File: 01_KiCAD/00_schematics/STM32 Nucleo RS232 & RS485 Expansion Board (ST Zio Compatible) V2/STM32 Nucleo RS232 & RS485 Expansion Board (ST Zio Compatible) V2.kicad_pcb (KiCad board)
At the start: 4 copper layers, 70 x 133.4 mm, 190 parts, among them CN10 Conn_02x17_Odd_Even, CN7 Conn_02x10_Odd_Even, CN8 Conn_02x08_Odd_Even, CN9 Conn_02x15_Odd_Even, IC1 REG103GA-A, J1 1190299, J10 DIR, J11 TERM_TX, J12 TERM_RX, J13 SLR, J2 CONN D-SUB PLUG 9POS TH, J3 TCVR_PWR, J4 TX_LED, J5 RX_LED, J6 SW_ENA, J7 MODE0, J8 MODE1, J9 MODE2, Q1 BSS84, Q2 BSS84, U1 TPS2117DRLR, U10 SN74LVC2G14DBV, U11 SN74LVC2G14DBV, U2 THVD4431RHAR, U3 SN74LVC2G14DBV, U4 SN74LVC245ADBR, U5 SN74LVC2G14DBV, U6 SN74LVC2G14DBV, U7 SN74LVC2G14DBV, U8 SN74LVC2G14DBV, U9 SN74LVC2G14DBV

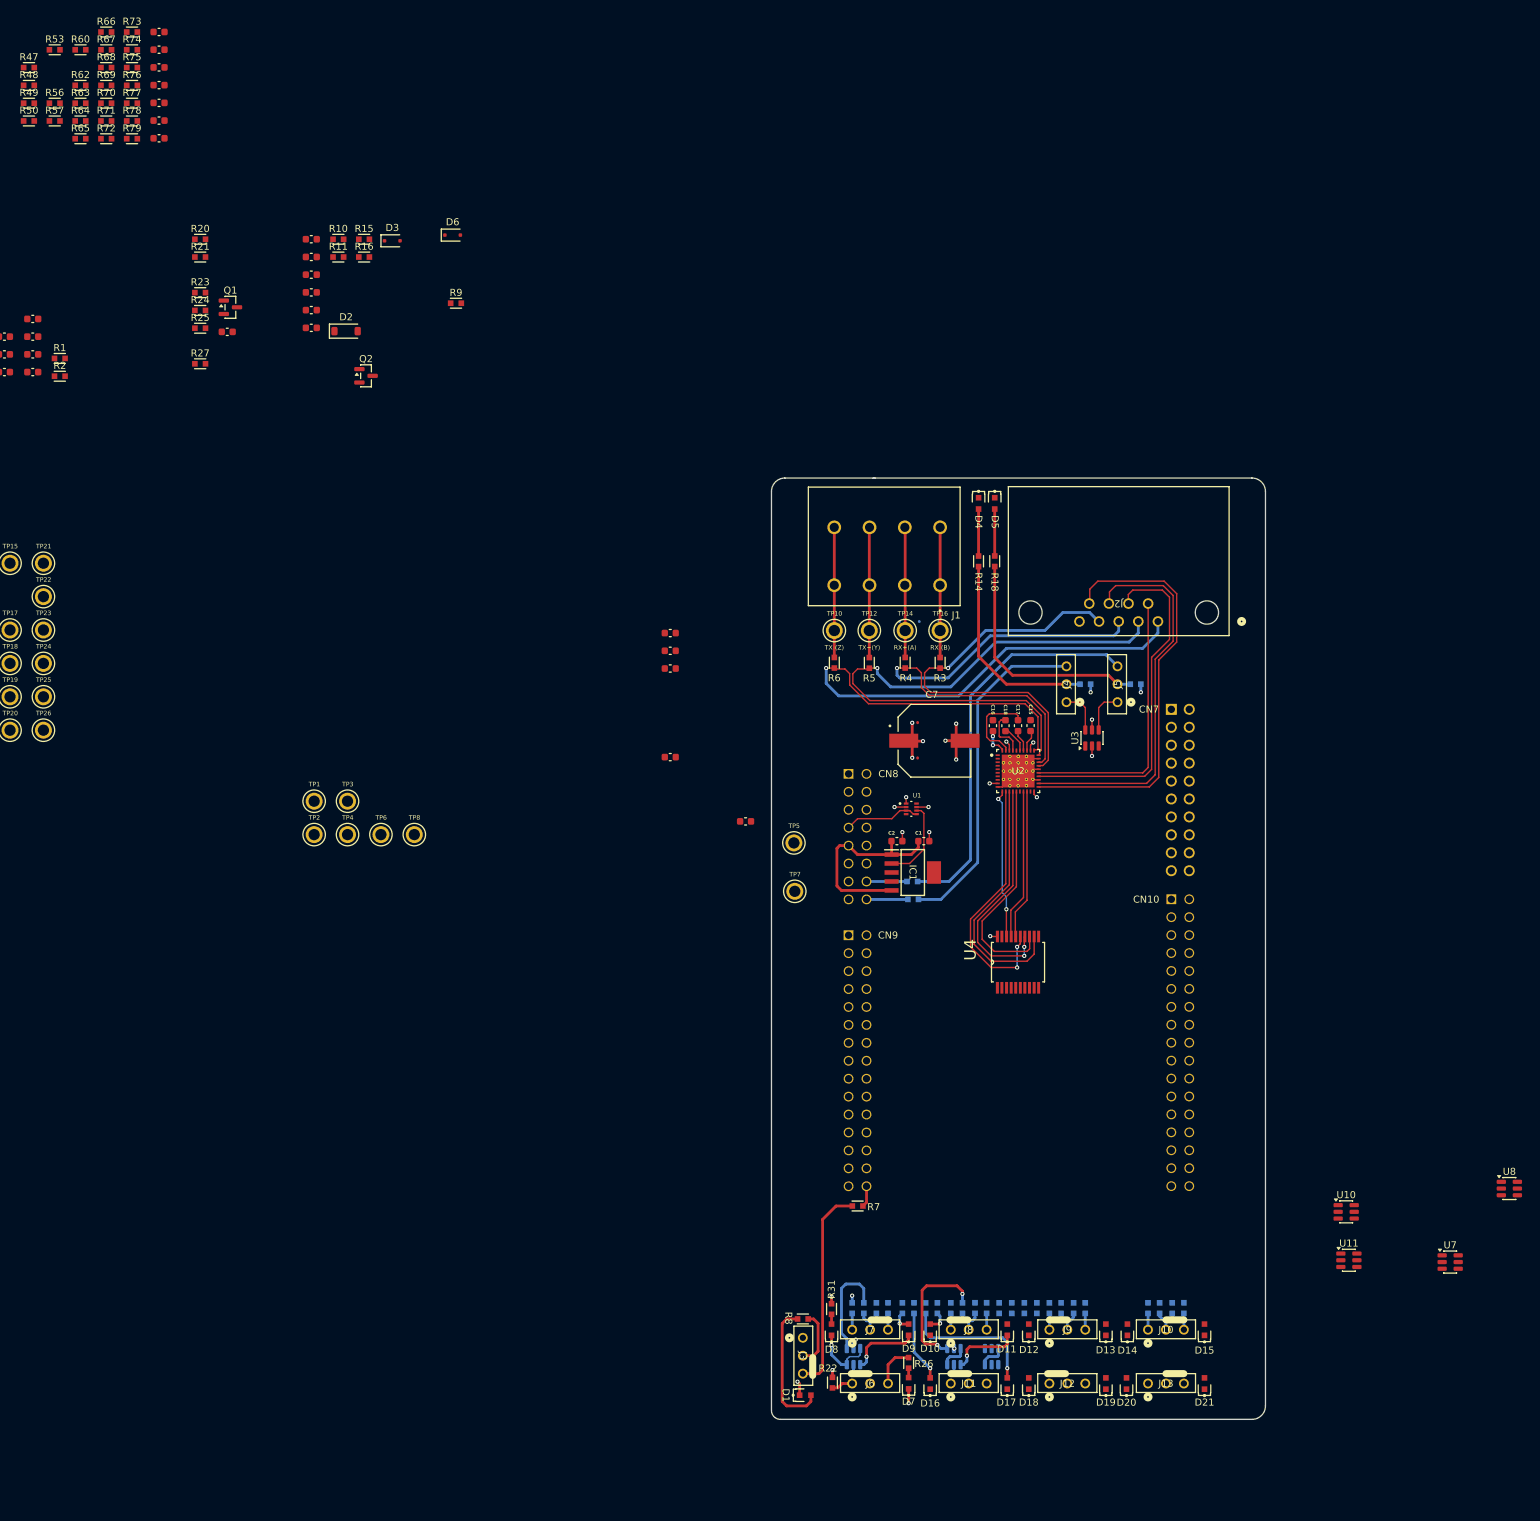
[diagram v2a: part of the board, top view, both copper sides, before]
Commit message: Changed to one-side only
Changed design to fit all components to top-side of the board inseatd of to both top- and bottom side of the board. This simplifies the manufacturing process and saves costs during assembly.
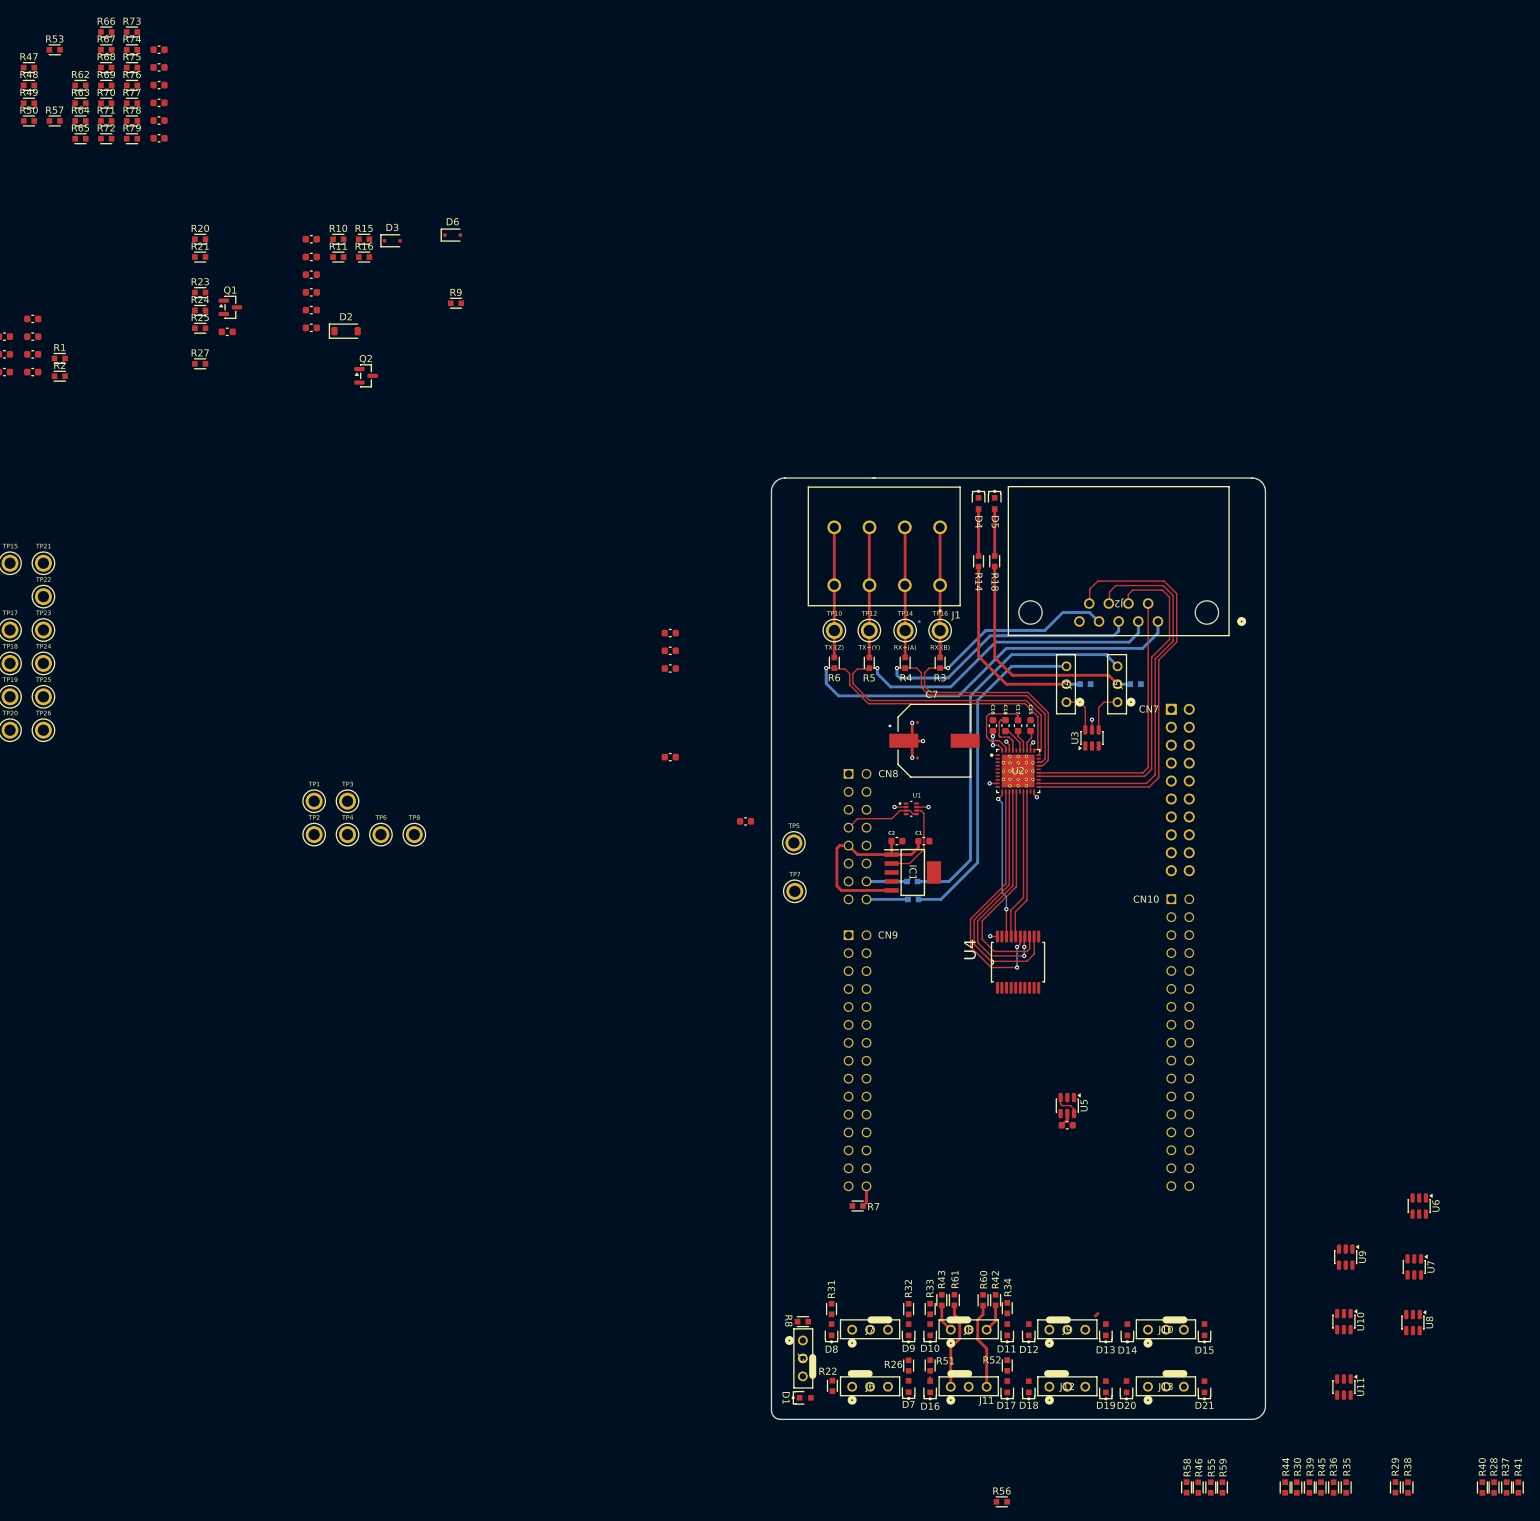
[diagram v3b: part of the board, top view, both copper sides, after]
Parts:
- R28, R29, R30, R32, R33, R34, R35, R36, R37, R38, R39, R40, R41, R42, R43, R44, R45, R46, R51, R52, R55, R58, R59, R61, U5, U6, U9: moved to F.Cu
- moved R56 239.3 mm to (69.5, 181.9)
- moved R60 218.5 mm to (66.8, 153.3), turned to -90 degrees
- moved C27 201.3 mm to (78.7, 128.5)
- moved R41 97.7 mm to (142.6, 179.8)
- moved R37 94.5 mm to (141.0, 179.8)
- moved R28 91.1 mm to (139.2, 179.8)
- moved R40 88.0 mm to (137.5, 179.8)
- moved U6 69.3 mm to (128.6, 140.0)
- moved R38 68.0 mm to (127.0, 179.8)
- moved R29 64.8 mm to (125.2, 179.8)
- moved R35 52.2 mm to (118.2, 179.8)
- moved U9 52.1 mm to (118.2, 147.2)
- moved R36 49.1 mm to (116.5, 179.8)
- moved U5 46.7 mm to (78.7, 125.7)
- moved R45 46.1 mm to (114.7, 179.8)
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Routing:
- net GND: track 31.9 -> 0.00 mm, vias 14 -> 0
- net Net-(J3-Pin_3): track 29.3 -> 0.00 mm
- net Net-(D17-A): track 19.9 -> 0.00 mm, vias 1 -> 0
- net Net-(U6-1A): track 19.1 -> 0.00 mm, vias 2 -> 0
- net Net-(D1-A): track 19.0 -> 0.00 mm
- net Net-(U5-1A): track 14.6 -> 0.00 mm
- net Net-(J11-Pin_1): track 0.00 -> 12.6 mm
- net Net-(J11-Pin_3): track 0.00 -> 12.3 mm
- net Net-(D9-K): track 10.1 -> 0.00 mm, vias 1 -> 0
- net Net-(D16-A): track 10.1 -> 0.05 mm, vias 1 -> 0
- net Net-(D11-K): track 10.0 -> 0.00 mm, vias 1 -> 0
- net /RS232 & RS485 Tranceiver/THVD_SHDN_N: track 8.03 -> 0.00 mm
- net MCU_OE: track 6.00 -> 0.00 mm
- net Net-(D8-K): track 9.30 -> 3.76 mm, vias 1 -> 0
- net MODE1: track 37.0 -> 32.3 mm
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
